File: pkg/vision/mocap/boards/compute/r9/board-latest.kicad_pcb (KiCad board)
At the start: 4 copper layers, 48 x 80 mm, 70 parts, among them J1 FH34SRJ-22S-0.5SH_50_, J10 AUX, J2 CAM_EXT_TRIG, J3 CAM_STROBE, J4 Conn_01x08, J5 SOLENOID, J6 PPS, J7 Conn_01x05, J9 10067099-200LF, Q2 BSS138, U1 STM32G031G4Ux, U10 DRV8837C, U2 TPS2378DDAR, U3 LM65645RZTR, U4 LIS2DW12TR, U5 TPD4EUSB30, U6 TPD4EUSB30, U7 MagJack-A70-112-331N126, U9 RT9742GGJ5, Y1 ASTX-H11-24.000MHZ-T

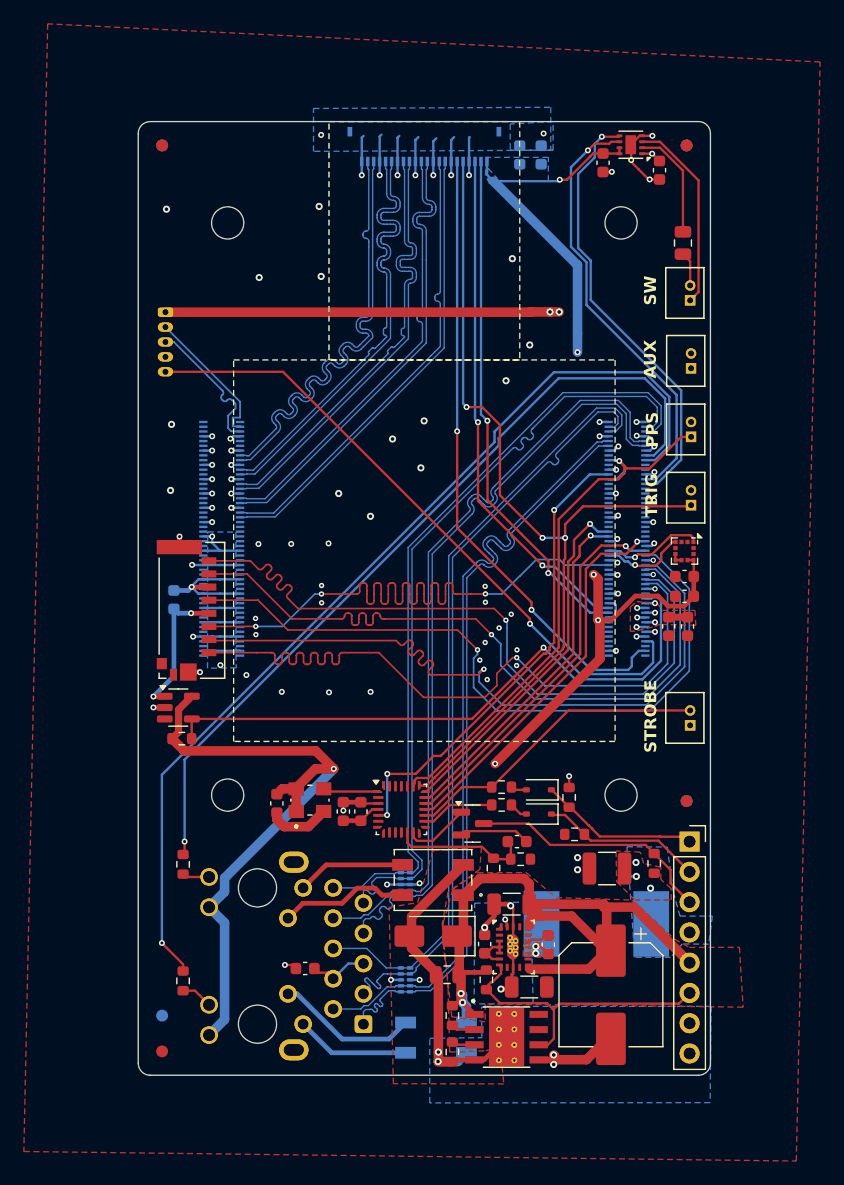
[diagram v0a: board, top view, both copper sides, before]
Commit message: New mocap compute board revisions.
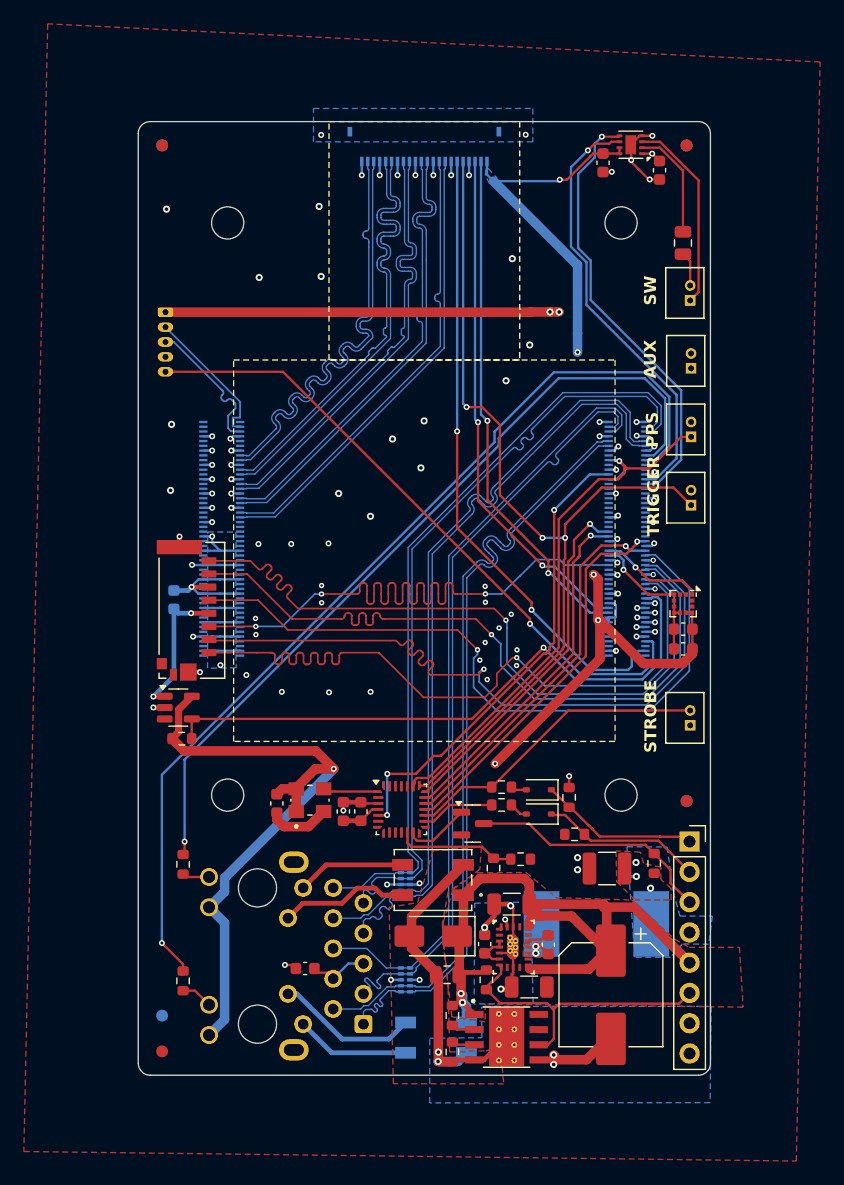
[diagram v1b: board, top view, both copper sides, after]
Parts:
- removed C10: 0.1uF 10V, Capacitor_SMD:C_0603_1608Metric
- removed C15: 1uF 10V, Capacitor_SMD:C_0603_1608Metric
- removed C16, C9: 0.1uF 6.6V, Capacitor_SMD:C_0603_1608Metric
- removed C17: 1uF 6.6V, Capacitor_SMD:C_0603_1608Metric
- R14: value 10K -> 1K
- R4: value 249K +/- 0.1% -> 24.9K +/- 0.1%
- R7: value 1K -> 10K
- R8: value 10K +/- 0.1% -> 1K +/- 0.1%
- moved C11 4.41 mm to (145.7, 142.6)
- moved C12 4.41 mm to (145.7, 144.2)
- moved U4 4.41 mm to (145.7, 140.4)
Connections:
- U3 pad 5: /5v_buck/BUCK_VCC -> GND
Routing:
- net GND: track 139.0 -> 121.9 mm
- net V_POE_SENSE: track 11.3 -> 9.74 mm
- net +5V: track 47.8 -> 46.3 mm
- net CM5_CAM_GPIO1: track 75.6 -> 76.8 mm
- net +3V3: track 169.2 -> 169.8 mm
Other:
- board text added: "Mocap Compute R9"
- board text added: "TRIGGER"
- board text removed: "Mocap Compute R10"
- board text removed: "TRIG"
